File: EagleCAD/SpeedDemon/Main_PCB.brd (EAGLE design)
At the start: 77.5 x 47.5 mm, 68 parts, among them Q1 DMC2700, U3 LM3676, U4 STM32F072-LQFP48, X1 32.768kHz

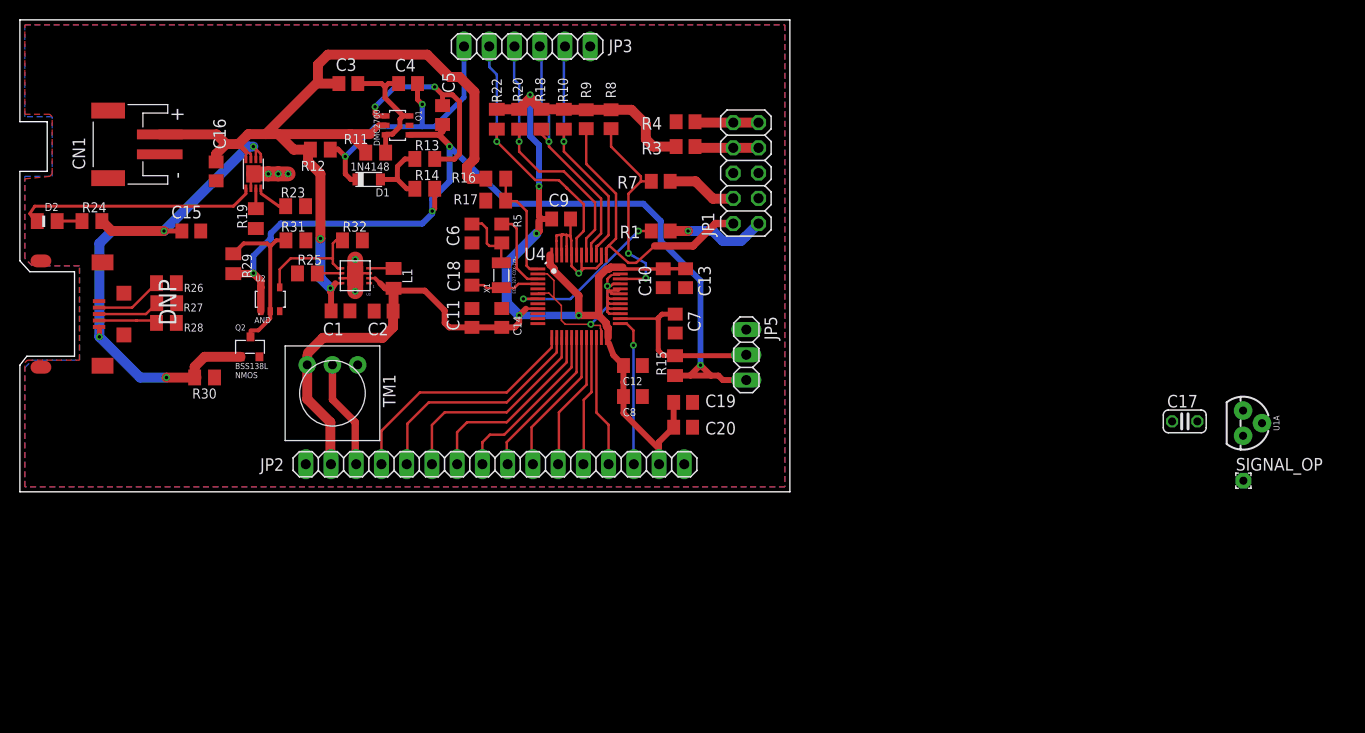
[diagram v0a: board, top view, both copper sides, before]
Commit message: Draft layout. Moved power reg circuit as far away from everything else as possible to minimize possible noise issues. Also poured polygons for power planes
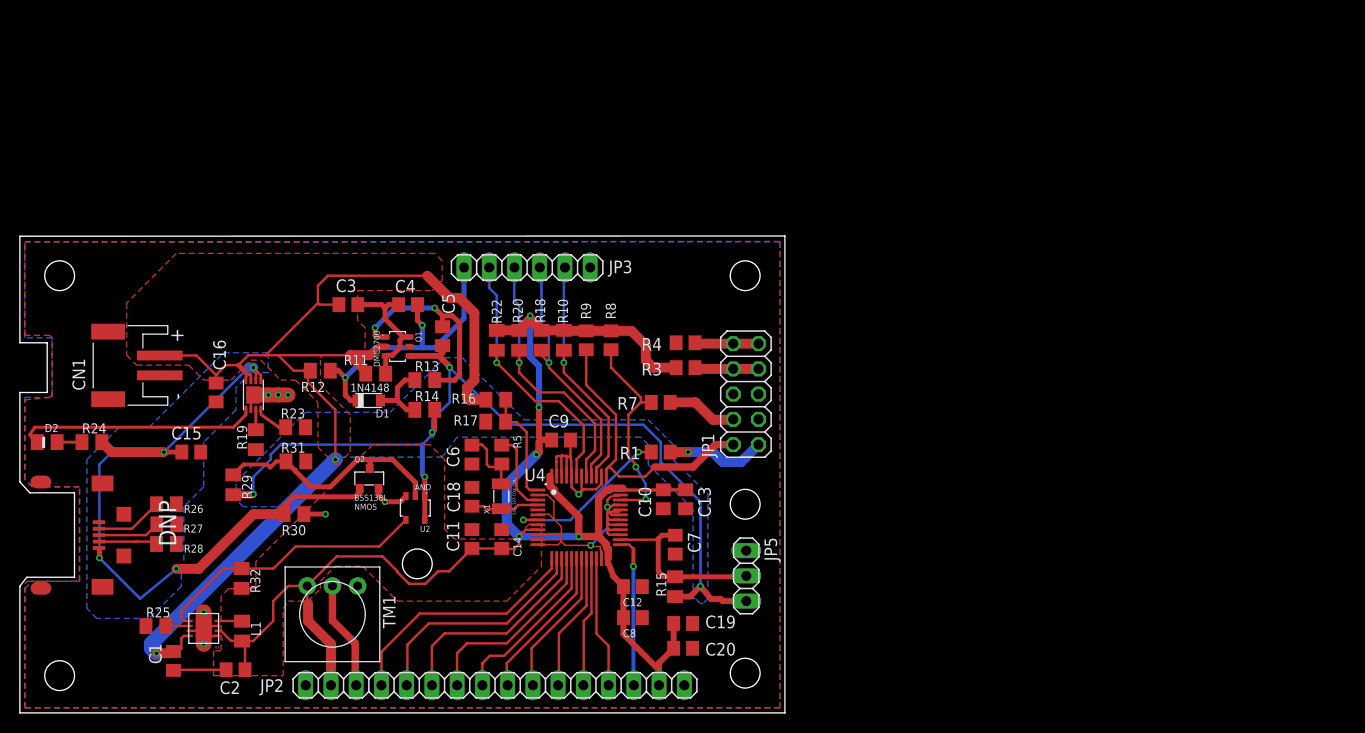
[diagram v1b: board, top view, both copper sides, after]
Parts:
- removed C17: 100nF, rcl:C025-024X044
- removed SIGNAL_OP: (no value), wirepad:1,6/0,8
- removed U1A: (no value), US5881:TO-92
- moved C2 39.1 mm to (21.7, 4.34)
- moved C1 39.0 mm to (15.5, 5.23), turned to 270 degrees
- moved L1 38.6 mm to (22.4, 8.23)
- moved R25 38.6 mm to (13.7, 8.73)
- moved U3 38.6 mm to (18.5, 8.50)
- moved R32 35.8 mm to (22.3, 13.5), turned to 270 degrees
- moved U2 25.6 mm to (39.8, 20.6), turned to 180 degrees
- moved R15 22.3 mm to (65.9, 12.7)
- moved R16 22.3 mm to (47.9, 31.5)
- moved R17 22.3 mm to (47.9, 29.3)
- moved R31 22.3 mm to (27.8, 25.3)
- moved C10 22.2 mm to (64.8, 21.5)
- moved C11 22.2 mm to (45.5, 17.5)
- moved C12 22.2 mm to (61.7, 12.7)
- moved C13 22.2 mm to (67.0, 21.5)
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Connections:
- removed net N$37: SIGNAL_OP.1, U1A.3
- net GND: no longer C17.2, U1A.2
- net VBATT+_SW: no longer C17.1, U1A.1
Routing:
- net VBATT+: track 94.3 -> 116.9 mm
- net GND: track 63.4 -> 83.8 mm, vias 8 -> 10
- net BATT_CHG_LOGIC_OP: track 11.8 -> 28.1 mm
- net +V+_CHG: track 59.2 -> 74.4 mm
- net +3V3: track 148.3 -> 157.1 mm
- net N$28: track 16.5 -> 24.7 mm
- net VBATT+_SW: track 94.3 -> 95.9 mm, vias 4 -> 5
- net FL_SWCLK: track 29.2 -> 28.7 mm
- added copper zone on layer 1, net +3V3
- added copper zone on layer 16, net +V+_CHG
- added copper zone on layer 1, net VBATT+
- added copper zone on layer 16, net VBATT+_SW
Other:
- board size 77.5 x 47.5 mm -> 77 x 48 mm

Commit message: fixed inductor choice, picked one that meets spec for the pwr converter
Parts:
- L1: value 2.2uH -> 2.2 uH; device 0805_generics:L_0805 -> LCRD_SMD_generics:NONSTANDARD_IND
- moved C2 2.50 mm to (19.2, 4.34)
- moved L1 1.52 mm to (23.2, 7.00), turned to 90 degrees
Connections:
- net +3V3: now also L1.P$1; no longer L1.2
- net N$10: now also L1.P$2; no longer L1.1
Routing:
- net +3V3: track 157.1 -> 162.0 mm
- net GND: track 83.8 -> 81.3 mm
- net N$10: track 2.75 -> 4.20 mm
- added copper zone on layer 1, net N$10
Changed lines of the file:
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@@
 <attribute name="VALUE" x="42.96" y="23.02" size="1.27" layer="27" rot="R270"/>
 </element>
-<element name="C2" library="0805_generics" package="C_0805" value="10uF" x="21.71" y="4.34" smashed="yes" rot="R180">
-<attribute name="NAME" x="20.1" y="1.9" size="1.27" layer="25"/>
-<attribute name="VALUE" x="22.98" y="6.88" size="1.27" layer="27" rot="R180"/>
+<element name="C2" library="0805_generics" package="C_0805" value="10uF" x="19.21" y="4.34" smashed="yes" rot="R180">
+<attribute name="NAME" x="17.6" y="1.9" size="1.27" layer="25"/>
+<attribute name="VALUE" x="20.48" y="6.88" size="1.27" layer="27" rot="R180"/>
 </element>
 <element name="C3" library="0805_generics" package="C_0805" value="100nF" x="33.06" y="41.09"/>
@@
 </element>
 <element name="JP5" library="pinhead" library_urn="urn:adsk.eagle:library:325" package="1X03" package3d_urn="urn:adsk.eagle:package:22458/2" value="" x="73.11" y="13.79" rot="R270"/>
-<element name="L1" library="0805_generics" package="L_0805" value="2.2uH" x="22.36" y="8.23" rot="R270"/>
 <element name="Q1" library="DMC2700" package="SOT-23-6" value="DMC2700" x="38.01" y="36.88" rot="R270"/>
 <element name="Q2" library="DMC2700" package="TO-236" value="" x="35.16" y="23.59" smashed="yes">
@@
 </element>
 <element name="U3" library="LM3676" package="WSON" value="LM3676" x="18.5" y="8.5" rot="R180"/>
+<element name="L1" library="LCRD_SMD_generics" package="NONSTANDARD_IND" value="2.2 uH" x="23.25" y="7" rot="R90"/>
 </elements>
 <signals>
@@
 <contactref element="R8" pad="2"/>
 <contactref element="C2" pad="1"/>
-<contactref element="L1" pad="2"/>
 <contactref element="U4" pad="24"/>
 <contactref element="C12" pad="1"/>
@@
 <wire x1="59.25" y1="22.43204375" x2="59.2861875" y2="22.43204375" width="0.75" layer="1"/>
 <wire x1="59.2861875" y1="22.43204375" x2="59.46154375" y2="22.6074" width="0.75" layer="1"/>
-<polygon width="0.2" layer="1">
+<polygon width="0.2" layer="1" rank="2">
 <vertex x="35.5" y="27"/>
 <vertex x="23.75" y="15.25"/>
@@
 <wire x1="29" y1="9.25" x2="31.31" y2="6.94" width="1" layer="1"/>
 <wire x1="31.31" y1="6.94" x2="31.31" y2="2.78" width="1" layer="1"/>
-<wire x1="22.36" y1="7.23" x2="23.48" y2="7.23" width="0.25" layer="1"/>
-<wire x1="25.5" y1="9.25" x2="25.5" y2="11.25" width="0.25" layer="1"/>
-<wire x1="25.5" y1="11.25" x2="27.0275" y2="12.7775" width="0.25" layer="1"/>
+<wire x1="26" y1="11.25" x2="26" y2="9.25" width="0.25" layer="1"/>
+<wire x1="26" y1="11.25" x2="27.0275" y2="12.7775" width="0.25" layer="1"/>
 <wire x1="27.0275" y1="12.7775" x2="28.92" y2="12.7775" width="0.25" layer="1"/>
-<wire x1="23.48" y1="7.23" x2="25.5" y2="9.25" width="0.25" layer="1"/>
-<wire x1="22.66" y1="4.34" x2="22.66" y2="6.93" width="0.25" layer="1"/>
-<wire x1="22.66" y1="6.93" x2="22.36" y2="7.23" width="0.25" layer="1"/>
 <wire x1="28.92" y1="12.7775" x2="31.8925" y2="15.75" width="0.25" layer="1"/>
 <wire x1="31.8925" y1="15.75" x2="36.5" y2="15.75" width="0.25" layer="1"/>
@@
 <wire x1="43.2" y1="14.25" x2="45.5" y2="16.55" width="0.25" layer="1"/>
 <wire x1="42.0869125" y1="14.25" x2="43.2" y2="14.25" width="0.25" layer="1"/>
-<wire x1="19.9" y1="8.25" x2="20.25" y2="8.25" width="0.25" layer="1"/>
-<wire x1="20.25" y1="8.25" x2="21.25" y2="7.25" width="0.25" layer="1"/>
-<wire x1="21.25" y1="7.25" x2="22.34" y2="7.25" width="0.25" layer="1"/>
-<wire x1="22.34" y1="7.25" x2="22.36" y2="7.23" width="0.25" layer="1"/>
+<wire x1="20.25" y1="8.25" x2="19.9" y2="8.25" width="0.25" layer="1"/>
 <wire x1="59.03" y1="15.53" x2="59.2074" y2="15.53" width="0.1524" layer="1"/>
 <wire x1="53.53" y1="23.83" x2="53.3526" y2="23.83" width="0.1524" layer="1"/>
+<contactref element="L1" pad="P$1"/>
+<wire x1="26" y1="9.25" x2="26" y2="7" width="0.2" layer="1"/>
+<wire x1="26" y1="7" x2="25.75" y2="6.75" width="0.2" layer="1"/>
+<wire x1="23.25" y1="6.5" x2="23.5" y2="6.75" width="0.2" layer="1"/>
+<wire x1="23.25" y1="5.6" x2="23.25" y2="6.5" width="0.2" layer="1"/>
+<wire x1="25.75" y1="6.75" x2="23.5" y2="6.75" width="0.2" layer="1"/>
+<wire x1="20.16" y1="4.34" x2="20.25" y2="4.25" width="0.2" layer="1"/>
+<wire x1="20.25" y1="4.25" x2="23.25" y2="4.25" width="0.2" layer="1"/>
+<wire x1="23.25" y1="4.25" x2="23.25" y2="5.6" width="0.2" layer="1"/>
+<wire x1="19.9" y1="8.25" x2="20.02259375" y2="8.12740625" width="0.2" layer="1"/>
+<wire x1="20.4524" y1="7.97955" x2="20.4524" y2="7.7976" width="0.2" layer="1"/>
+<wire x1="20.02259375" y1="8.12740625" x2="20.30454375" y2="8.12740625" width="0.2" layer="1"/>
+<wire x1="20.30454375" y1="8.12740625" x2="20.4524" y2="7.97955" width="0.2" layer="1"/>
+<wire x1="21.75" y1="6.5" x2="23.25" y2="6.5" width="0.2" layer="1"/>
+<wire x1="20.4524" y1="7.7976" x2="21.75" y2="6.5" width="0.2" layer="1"/>
 </signal>
 <signal name="+5V">
@@
 <wire x1="23.25" y1="31.5" x2="23.5" y2="31.75" width="0.25" layer="1"/>
 <wire x1="23.5" y1="31.75" x2="23.5" y2="32" width="0.25" layer="1"/>
-<polygon width="0.25" layer="1" rank="2">
+<polygon width="0.25" layer="1" rank="3">
 <vertex x="0.5" y="23.5"/>
 <vertex x="0.5" y="31.5"/>
@@
 <wire x1="58.5" y1="18" x2="59.131628125" y2="18.631628125" width="0.25" layer="16"/>
 <wire x1="59.131628125" y1="18.631628125" x2="59.131628125" y2="20.710375" width="0.25" layer="16"/>
-<wire x1="20.76" y1="4.34" x2="15.52" y2="4.34" width="0.25" layer="1"/>
+<wire x1="18.26" y1="4.34" x2="15.52" y2="4.34" width="0.25" layer="1"/>
 <wire x1="15.52" y1="4.34" x2="15.46" y2="4.28" width="0.25" layer="1"/>
 <wire x1="38.85" y1="21.82" x2="38.28" y2="21.25" width="0.5" layer="1"/>
@@
 </signal>
 <signal name="N$10">
-<contactref element="L1" pad="1"/>
-<wire x1="22.36" y1="9.23" x2="22.27" y2="9.14" width="0.25" layer="1"/>
 <contactref element="U3" pad="FB"/>
-<wire x1="22.16" y1="9.25" x2="22.27" y2="9.14" width="0.25" layer="1"/>
-<wire x1="19.9" y1="9.25" x2="22.34" y2="9.25" width="0.25" layer="1"/>
-<wire x1="22.34" y1="9.25" x2="22.36" y2="9.23" width="0.25" layer="1"/>
+<contactref element="L1" pad="P$2"/>
+<polygon width="0.2" layer="1">
+<vertex x="20" y="9.25"/>
+<vertex x="20.25" y="9.5"/>
+<vertex x="25.5" y="9.5"/>
+<vertex x="25.5" y="7.25"/>
+<vertex x="21.75" y="7.25"/>
+<vertex x="20.25" y="9.25"/>
+</polygon>
+<wire x1="19.9" y1="9.25" x2="23.25" y2="9.25" width="0.2" layer="1"/>
+<wire x1="23.25" y1="9.25" x2="23.25" y2="8.4" width="0.2" layer="1"/>
 </signal>
 <signal name="Q1_D1">

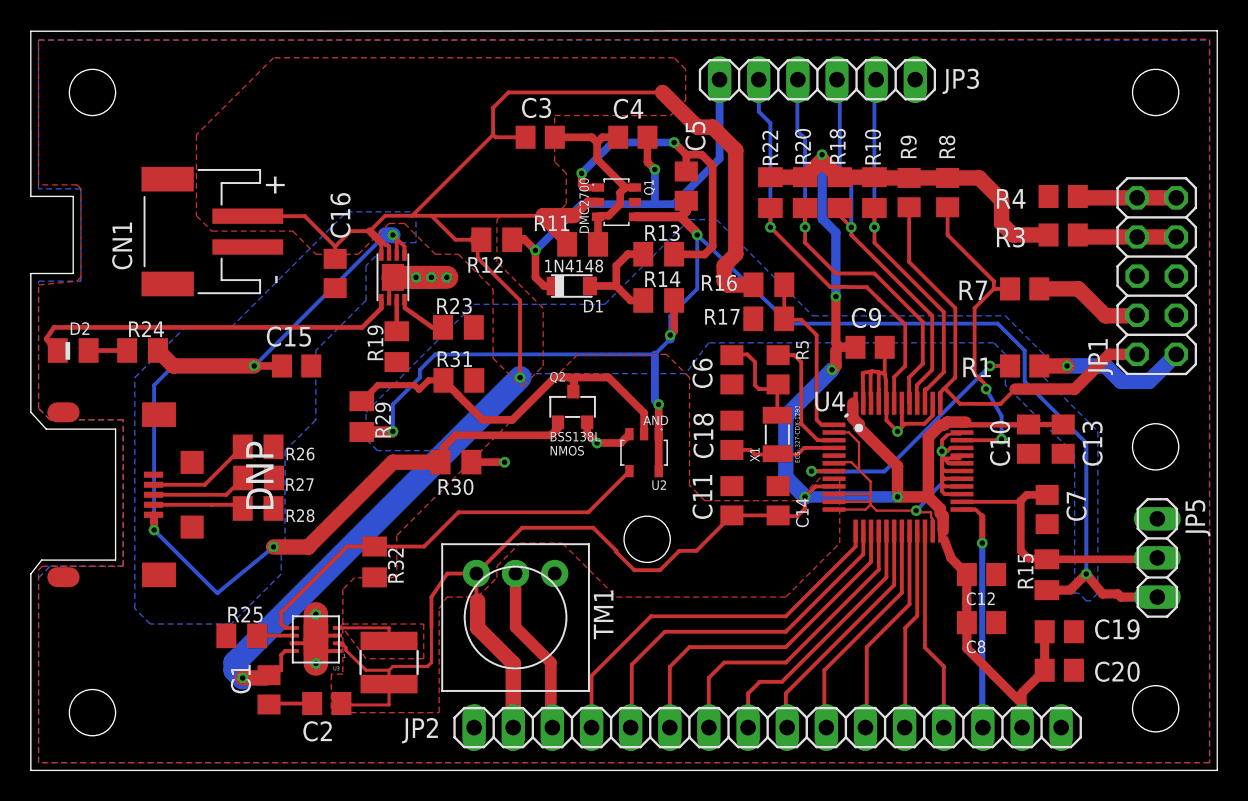
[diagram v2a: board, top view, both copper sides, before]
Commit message: Fixed several DRC errors
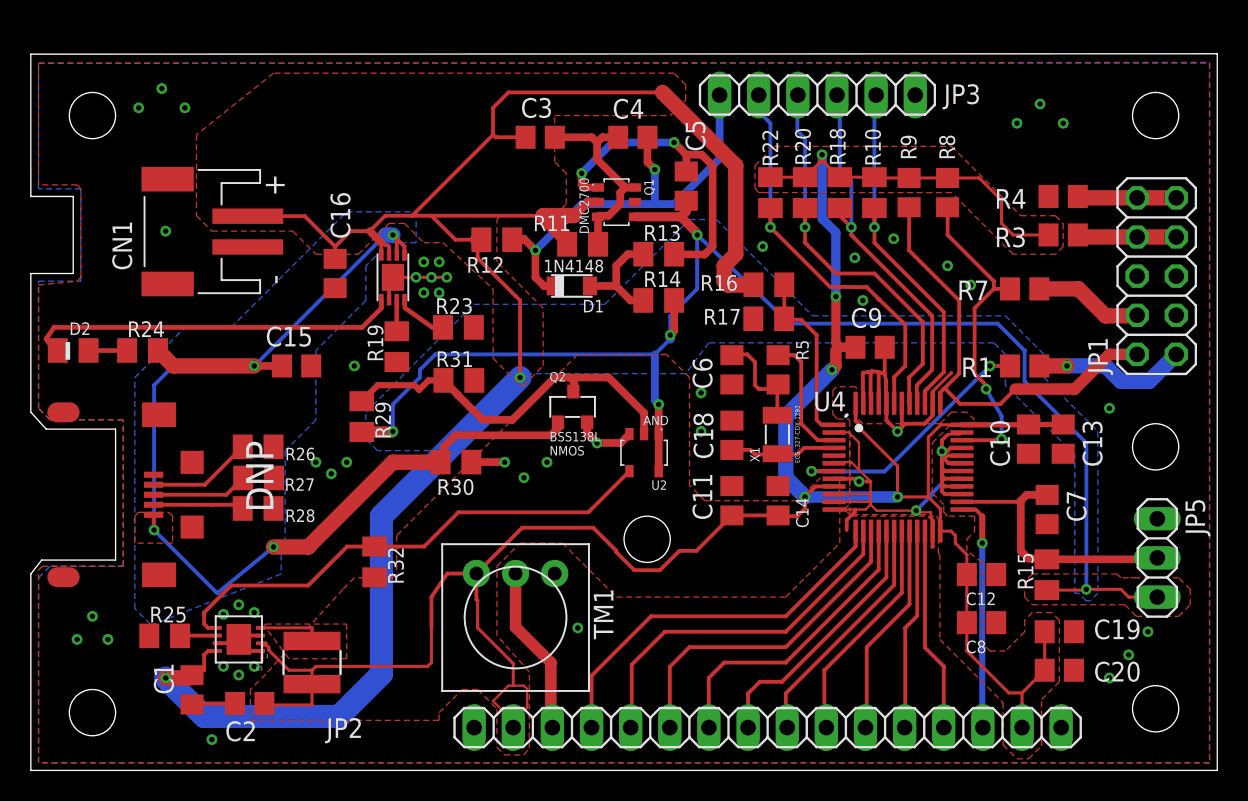
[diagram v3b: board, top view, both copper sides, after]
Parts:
- moved C1 5.00 mm to (10.5, 5.23)
- moved C2 5.00 mm to (14.2, 4.34)
- moved L1 5.00 mm to (18.2, 7.00)
- moved R25 5.00 mm to (8.69, 8.73)
- moved U3 5.00 mm to (13.5, 8.50)
- moved JP3 1.00 mm to (51.0, 43.8)
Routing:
- net VBATT+: track 116.9 -> 128.1 mm
- net +3V3: track 162.0 -> 169.5 mm
- net BATT_CHG_LOGIC_OP: track 28.1 -> 33.1 mm
- net GND: track 81.3 -> 85.2 mm, vias 10 -> 49
- net PWR_SW: track 29.1 -> 28.1 mm
- net SW_LEFT: track 28.1 -> 29.1 mm
- net SW_RIGHT: track 27.5 -> 28.4 mm
- net SW_UP: track 24.7 -> 25.4 mm
- net SW_DOWN: track 25.5 -> 26.1 mm
- added copper zone on layer 1, net +V+_CHG
- added copper zone on layer 1, net VBATT+_SW
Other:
- board size 77 x 48 mm -> 77 x 46.5 mm

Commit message: HW5 added
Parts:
- moved TM1 3.01 mm to (31.7, 12.9), turned to 90 degrees
- moved U2 1.77 mm to (39.5, 22.4)
- moved R32 0.75 mm to (21.6, 13.5)
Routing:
- net GND: track 85.2 -> 113.4 mm, vias 49 -> 56
- net +3V3: track 169.5 -> 163.8 mm
- net +V+_CHG: track 74.4 -> 71.8 mm
- net N$28: track 24.7 -> 22.9 mm
- net VBATT+: track 128.1 -> 129.9 mm
- net BATT_CHG_LOGIC_OP: track 33.1 -> 34.7 mm
- net VBATT+_SW: track 96.0 -> 95.0 mm
- net N$14: track 11.0 -> 11.7 mm
- added copper zone on layer 16, net VBATT+
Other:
- board text added: "L.H. A.C."
- board text added: "Speed Demon -- Main PCB Team 15"
- board text added: "Z.S. N.D."
